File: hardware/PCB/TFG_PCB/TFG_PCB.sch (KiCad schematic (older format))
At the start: 0 parts

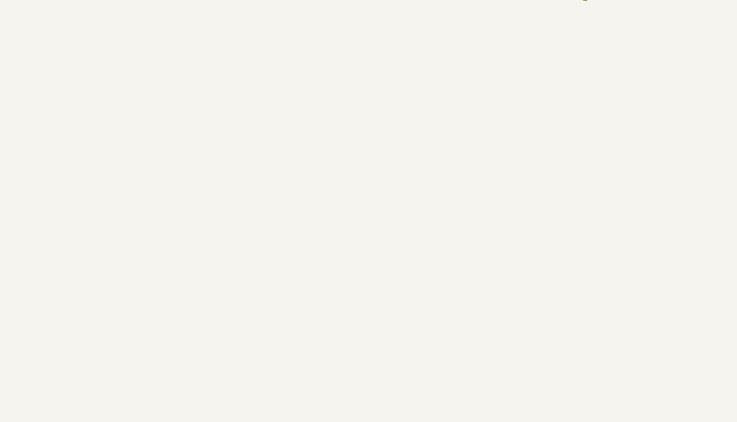
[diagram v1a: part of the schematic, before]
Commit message: netlist and Motor Control sheet
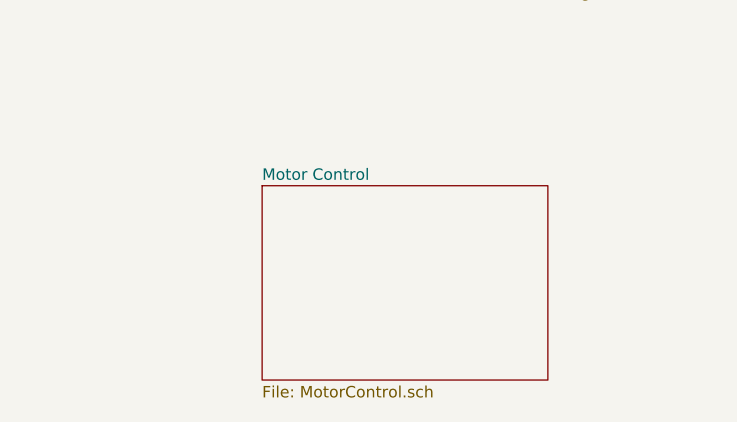
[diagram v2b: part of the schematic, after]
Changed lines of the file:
@@
 F4 "ALG_BUS" O L 6050 2550 50
 $EndSheet
+$Sheet
+S 5150 3550 1250 850
+U 5E691C3E
+F0 "Motor Control" 50
+F1 "MotorControl.sch" 50
+$EndSheet
 $EndSCHEMATC

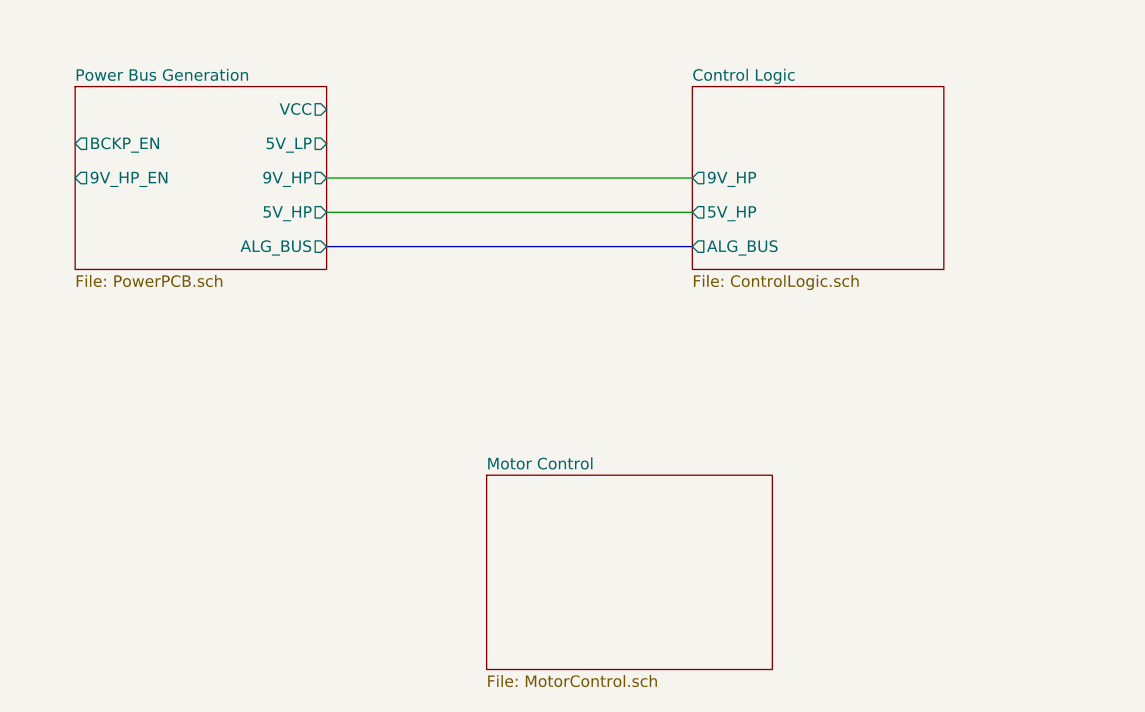
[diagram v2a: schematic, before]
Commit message: Updated netlist and footprints
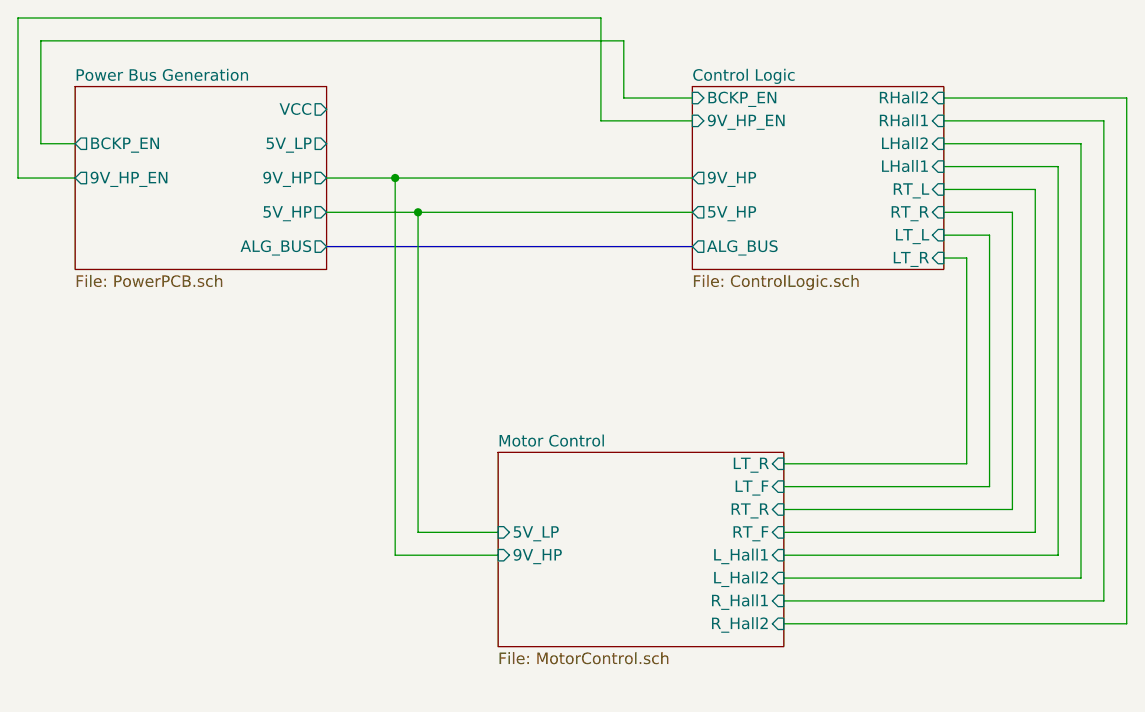
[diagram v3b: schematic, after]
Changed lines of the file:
@@
 $Descr A4 11693 8268
 encoding utf-8
-Sheet 1 3
+Sheet 1 4
 Title "ROVER Main PCB"
 Date "2020-01-24"
@@
 $EndSheet
 Wire Wire Line
-	6050 2250 4450 2250
-Wire Wire Line
-	4450 2400 6050 2400
+	4450 2400 4850 2400
 Wire Bus Line
 	4450 2550 6050 2550
+$Sheet
+S 5200 3450 1250 850
+U 5E691C3E
+F0 "Motor Control" 50
+F1 "MotorControl.sch" 50
+F2 "9V_HP" I L 5200 3900 50
+F3 "LT_R" I R 6450 3500 50
+F4 "LT_F" I R 6450 3600 50
+F5 "RT_R" I R 6450 3700 50
+F6 "RT_F" I R 6450 3800 50
+F7 "L_Hall1" I R 6450 3900 50
+F8 "L_Hall2" I R 6450 4000 50
+F9 "R_Hall1" I R 6450 4100 50
+F10 "R_Hall2" I R 6450 4200 50
+F11 "5V_LP" I L 5200 3800 50
+$EndSheet
+Wire Wire Line
+	4450 2250 4750 2250
+Wire Wire Line
+	5200 3800 4850 3800
+Wire Wire Line
+	4850 3800 4850 2400
+Connection ~ 4850 2400
+Wire Wire Line
+	4850 2400 6050 2400
+Wire Wire Line
+	5200 3900 4750 3900
+Wire Wire Line
+	4750 3900 4750 2250
+Connection ~ 4750 2250
+Wire Wire Line
+	4750 2250 6050 2250
 $Sheet
 S 6050 1850 1100 800
@@
 F3 "9V_HP" O L 6050 2250 50
 F4 "ALG_BUS" O L 6050 2550 50
+F5 "LT_R" I R 7150 2600 50
+F6 "LT_L" I R 7150 2500 50
+F7 "RT_R" I R 7150 2400 50
+F8 "RT_L" I R 7150 2300 50
+F9 "LHall1" I R 7150 2200 50
+F10 "LHall2" I R 7150 2100 50
+F11 "RHall1" I R 7150 2000 50
+F12 "RHall2" I R 7150 1900 50
+F13 "BCKP_EN" I L 6050 1900 50
+F14 "9V_HP_EN" I L 6050 2000 50
 $EndSheet
-$Sheet
-S 5150 3550 1250 850
-U 5E691C3E
-F0 "Motor Control" 50
-F1 "MotorControl.sch" 50
-$EndSheet
+Wire Wire Line
+	7150 2600 7250 2600
+Wire Wire Line
+	7250 2600 7250 3500
+Wire Wire Line
+	7250 3500 6450 3500
+Wire Wire Line
+	6450 3600 7350 3600
+Wire Wire Line
+	7350 3600 7350 2500
+Wire Wire Line
+	7350 2500 7150 2500
+Wire Wire Line
+	7150 2400 7450 2400
+Wire Wire Line
+	7450 2400 7450 3700
+Wire Wire Line
+	7450 3700 6450 3700
+Wire Wire Line
+	6450 3800 7550 3800
+Wire Wire Line
+	7550 3800 7550 2300
+Wire Wire Line
+	7550 2300 7150 2300
+Wire Wire Line
+	7150 2200 7650 2200
+Wire Wire Line
+	7650 2200 7650 3900
+Wire Wire Line
+	7650 3900 6450 3900
+Wire Wire Line
+	6450 4000 7750 4000
+Wire Wire Line
+	7750 4000 7750 2100
+Wire Wire Line
+	7750 2100 7150 2100
+Wire Wire Line
+	7150 2000 7850 2000
+Wire Wire Line
+	7850 2000 7850 4100
+Wire Wire Line
+	7850 4100 6450 4100
+Wire Wire Line
+	6450 4200 7950 4200
+Wire Wire Line
+	7950 4200 7950 1900
+Wire Wire Line
+	7950 1900 7150 1900
+Wire Wire Line
+	3350 2100 3200 2100
+Wire Wire Line
+	3200 2100 3200 1650
+Wire Wire Line
+	3200 1650 5750 1650
+Wire Wire Line
+	5750 1650 5750 1900
+Wire Wire Line
+	5750 1900 6050 1900
+Wire Wire Line
+	6050 2000 5650 2000
+Wire Wire Line
+	5650 2000 5650 1550
+Wire Wire Line
+	5650 1550 3100 1550
+Wire Wire Line
+	3100 1550 3100 2250
+Wire Wire Line
+	3100 2250 3350 2250
 $EndSCHEMATC
